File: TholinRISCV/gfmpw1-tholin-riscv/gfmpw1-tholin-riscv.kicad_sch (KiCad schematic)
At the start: 35 parts, among them J1 Screw_Terminal_01x02, J2 Conn_01x06, J3 Micro_SD_Card, J4 Conn_01x06, J5 Conn_02x05_Counter_Clockwise, J6 Conn_01x03, SW1 SW_Push, SW2 SW_Push, U1 gfmpw1-multi, U10 74LS08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

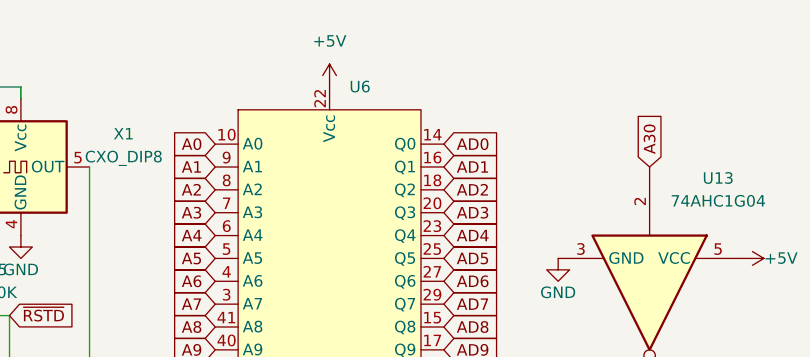
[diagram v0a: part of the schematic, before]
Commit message: RISCV: TCP support in network stack.
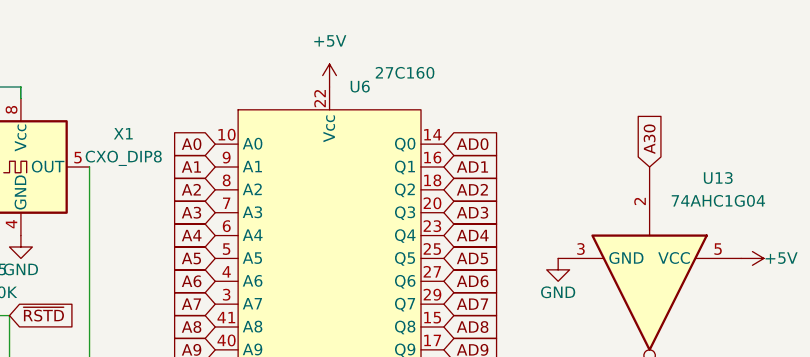
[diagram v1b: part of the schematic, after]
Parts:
- U6: value ~ -> 27C160
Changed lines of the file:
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@@
 		(on_board yes)
 		(dnp no)
-		(fields_autoplaced yes)
 		(property "Reference" "U6"
 			(at 110.1441 20.32 0)
@@
 			)
 		)
-		(property "Value" "~"
-			(at 107.95 19.05 0)
+		(property "Value" "27C160"
+			(at 116.332 18.796 0)
 			(effects
 				(font
